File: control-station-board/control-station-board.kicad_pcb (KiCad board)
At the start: 2 copper layers, 9.7 x 10.3 mm, 41 parts, among them J1 USB_B, J2 USB_B, J3 CAM1_OUT, J4 CAM2_OUT, U1 MAX4445, U2 LTC1983ES6-5-TRPBF, U3 MAX4445, U4 THVD1550DR, U5 FT232RL, U6 ATA6560,1, U7 FT232RL

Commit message: working on pcb layout
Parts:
- removed R5, R6: 10k, Resistor_SMD:R_0603_1608Metric
- J1, J2: footprint Connector_USB:USB_B_OST_USB-B1HSxx_Horizontal -> Connector_USB:USB_B_TE_5787834_Vertical
- U4: value THVD1550DR -> MAX490E
- moved J3 137.7 mm to (168.6, 96.4), turned to 0 degrees
- moved J4 137.7 mm to (168.6, 80.4), turned to 0 degrees
- moved C6 117.4 mm to (155.8, 69.4), turned to 270 degrees
- moved C2 116.0 mm to (157.1, 99.7), turned to 270 degrees
- moved R3 115.9 mm to (157.0, 76.9), turned to 90 degrees
- moved R4 115.4 mm to (156.3, 74.6), turned to 180 degrees
- moved C4 114.3 mm to (155.1, 72.4), turned to 0 degrees
- moved R1 114.0 mm to (157.0, 93.1), turned to 90 degrees
- moved C7 114.0 mm to (157.0, 83.5), turned to 270 degrees
- moved R2 112.2 mm to (156.3, 90.8), turned to 180 degrees
- moved U2 112.0 mm to (153.0, 69.4), turned to 90 degrees
- moved C3 106.4 mm to (150.0, 69.5), turned to 90 degrees
- moved U1 105.7 mm to (152.3, 97.0), turned to 0 degrees
- moved U3 105.2 mm to (152.3, 80.9), turned to 0 degrees
- moved C5 104.0 mm to (150.4, 74.6), turned to 0 degrees
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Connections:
- R7 pad 1: RS485_B -> RX_H
- R7 pad 2: RS485_A -> RX_L
- U4 pad 1: R -> +5V
- U4 pad 2: Net-(R5-Pad1) -> R
- U4 pad 3: Net-(R6-Pad2) -> D
- U4 pad 4: D -> GND
- U4 pad 5: GND -> TX_H
- U4 pad 6: RS485_A -> TX_L
- U4 pad 7: RS485_B -> RX_L
- U4 pad 8: +5V -> RX_H
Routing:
- net GND: track 24.3 -> 26.8 mm
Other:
- board size 9.7 x 10.3 mm -> 76.2 x 44.5 mm

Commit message: Finishing pcb routing
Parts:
- added J5: USB D+/D-, Connector_PinHeader_2.54mm:PinHeader_1x02_P2.54mm_Vertical, F.Cu at (104.3, 90.6)
- added J6: Conn_02x06_Odd_Even, Connector_PinHeader_2.54mm:PinHeader_2x06_P2.54mm_Vertical, F.Cu at (104.3, 74.7)
- moved C6 37.8 mm to (149.6, 106.7), turned to 90 degrees
- moved R12 37.7 mm to (121.3, 94.0), turned to 180 degrees
- moved C3 37.5 mm to (155.5, 106.6), turned to 270 degrees
- moved D3 37.5 mm to (124.5, 94.0), turned to 0 degrees
- moved U2 37.3 mm to (152.5, 106.7), turned to 270 degrees
- moved R8 34.9 mm to (138.5, 94.1), turned to 180 degrees
- moved R13 33.4 mm to (121.4, 95.7), turned to 180 degrees
- moved D4 33.4 mm to (124.5, 95.7), turned to 0 degrees
- moved C4 31.7 mm to (150.3, 103.7), turned to 180 degrees
- moved R9 31.0 mm to (138.6, 95.6), turned to 180 degrees
- moved D1 30.5 mm to (141.8, 94.1), turned to 0 degrees
- moved D2 25.1 mm to (141.8, 95.6), turned to 0 degrees
- moved R10 24.4 mm to (120.8, 76.7), turned to 0 degrees
- moved C8 24.2 mm to (144.3, 81.4)
- moved R11 24.0 mm to (118.1, 80.4), turned to 90 degrees
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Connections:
- U5 pad 1: R -> D
- U5 pad 5: D -> R
- U7 pad 1: RXD -> TXD
- U7 pad 5: TXD -> RXD
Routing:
- net +5V: track 49.5 -> 208.3 mm, vias 5 -> 17
- net CAM1+: track 0.00 -> 64.4 mm, vias 0 -> 2
- net CAM1-: track 0.00 -> 63.1 mm, vias 0 -> 2
- net CAM2+: track 0.00 -> 53.7 mm, vias 0 -> 2
- net CAM2-: track 0.00 -> 50.3 mm, vias 0 -> 2
- net GND: track 26.8 -> 75.7 mm, vias 0 -> 44
- net RX_H: track 0.00 -> 32.4 mm, vias 0 -> 1
- net RX_L: track 0.00 -> 32.0 mm, vias 0 -> 1
- net TX_L: track 0.00 -> 31.3 mm, vias 0 -> 1
- net TX_H: track 0.00 -> 31.0 mm, vias 0 -> 1
- net CANL: track 0.00 -> 15.5 mm, vias 0 -> 1
- net CANH: track 0.00 -> 15.0 mm, vias 0 -> 1
- net Net-(J1-Pad3): track 0.00 -> 12.7 mm
- net Net-(J2-Pad3): track 0.00 -> 12.7 mm
- net Net-(J2-Pad2): track 0.00 -> 9.10 mm
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- added copper zone on B.Cu, net GND
- added copper zone on F.Cu, net GND
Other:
- board size 76.2 x 44.5 mm -> 68.6 x 43.8 mm

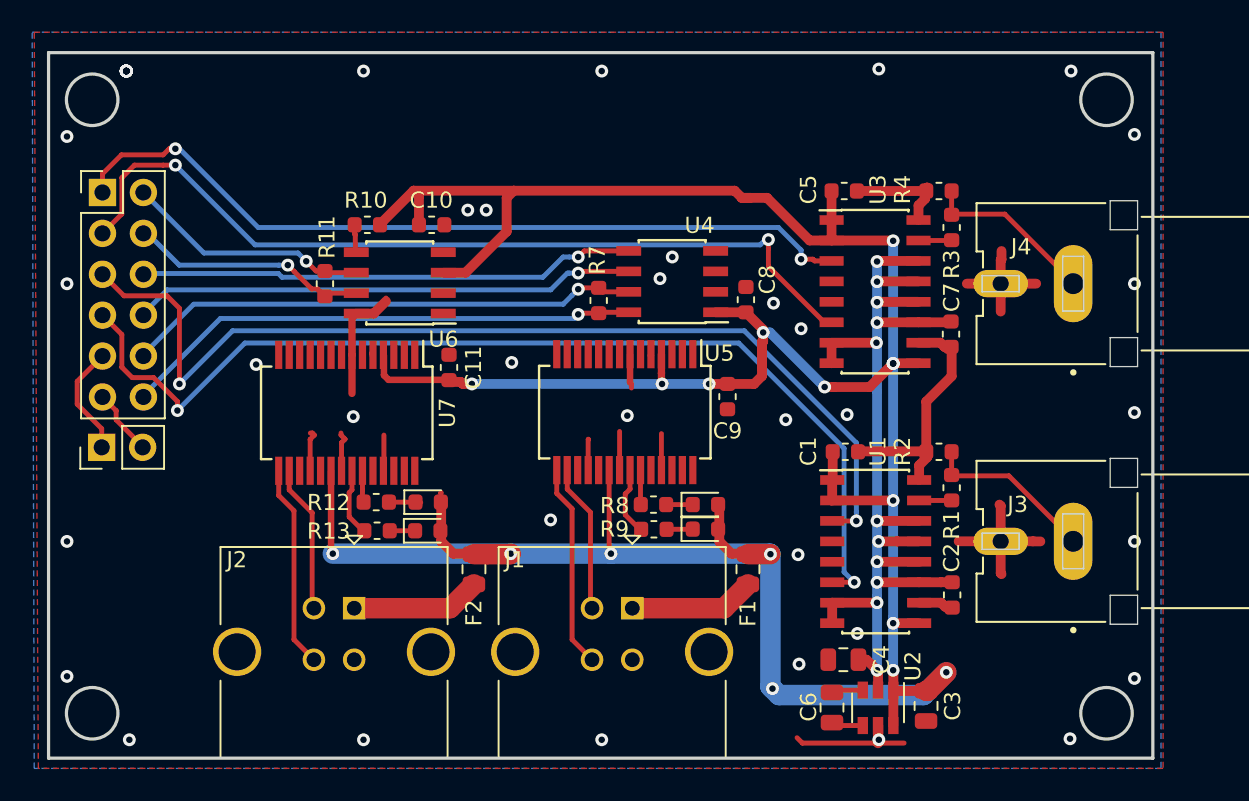
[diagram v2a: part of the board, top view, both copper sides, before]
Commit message: Finished PCB routing and silkscreen
Created 3d model,
Created gerber files
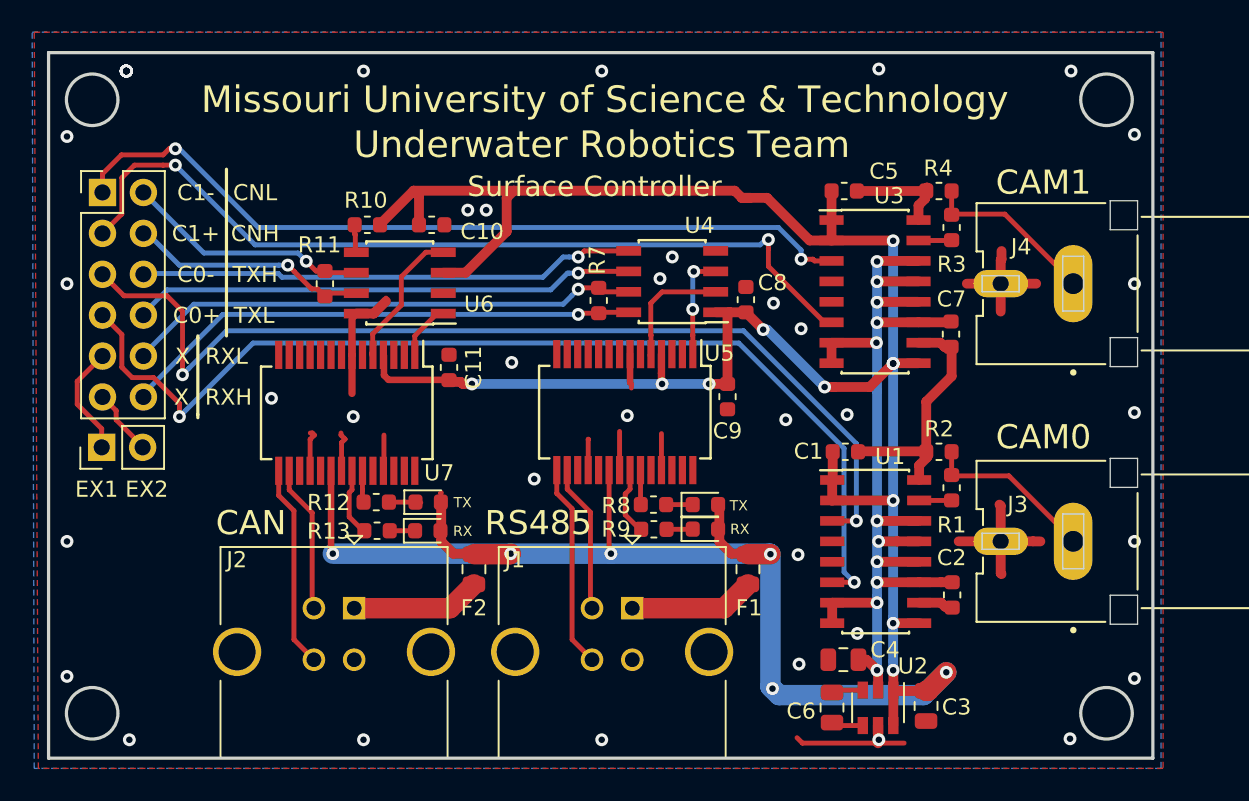
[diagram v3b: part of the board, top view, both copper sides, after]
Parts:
- J3: value CAM1_OUT -> CAM0_OUT
- J4: value CAM2_OUT -> CAM1_OUT
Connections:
- J3 pad 1: CAM1_OUT -> CAM0_OUT
- J4 pad 1: CAM2_OUT -> CAM1_OUT
- J6 pad 1: CAM2- -> CAM1-
- J6 pad 3: CAM2+ -> CAM1+
- J6 pad 5: CAM1- -> CAM0-
- J6 pad 7: CAM1+ -> CAM0+
- R1 pad 2: CAM1_OUT -> CAM0_OUT
- R2 pad 1: CAM1_OUT -> CAM0_OUT
- R3 pad 2: CAM2_OUT -> CAM1_OUT
- R4 pad 1: CAM2_OUT -> CAM1_OUT
- U1 pad 3: CAM1- -> CAM0-
- U1 pad 6: CAM1+ -> CAM0+
- U3 pad 3: CAM2- -> CAM1-
- U3 pad 6: CAM2+ -> CAM1+
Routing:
- net CAM0+: track 0.00 -> 64.9 mm, vias 0 -> 2
- net CAM0-: track 0.00 -> 62.2 mm, vias 0 -> 2
- net CAM2+: track 53.7 -> 0.00 mm, vias 2 -> 0
- net CAM2-: track 50.3 -> 0.00 mm, vias 2 -> 0
- net CAM1-: track 63.1 -> 50.3 mm
- net CAM2_OUT: track 10.8 -> 0.00 mm
- net CAM0_OUT: track 0.00 -> 10.8 mm
- net CAM1+: track 64.4 -> 53.7 mm
- net RXD: track 0.30 -> 9.09 mm
- net R: track 0.13 -> 7.65 mm
- net D: track 0.00 -> 6.63 mm, vias 0 -> 2
- net TXD: track 0.00 -> 3.46 mm
- net +5V: track 208.3 -> 206.0 mm
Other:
- board text added: "C0+"
- board text added: "C0-"
- board text added: "C1+"
- board text added: "C1-"
- board text added: "CAM0"
- board text added: "CAM1"
- board text added: "CAN"
- board text added: "CNH"
- board text added: "CNL"
- board text added: "EX1"
- board text added: "EX2"
- board text added: "Missouri University of Science & Technology"
- board text added: "RS485"
- board text added: "RX"
- board text added: "RXH"
- board text added: "RXL"
- board text added: "Surface Controller"
- board text added: "TX"
- board text added: "TXH"
- board text added: "TXL"
- board text added: "Underwater Robotics Team"
- board text added: "X"

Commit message: Exported gerber files for surface control board
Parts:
- added REF**: MountingHole_3.2mm_M3, MountingHole:MountingHole_3.2mm_M3, F.Cu at (103.7, 107.1)
- added REF**: MountingHole_3.2mm_M3, MountingHole:MountingHole_3.2mm_M3, F.Cu at (166.7, 107.1)
- added REF**: MountingHole_3.2mm_M3, MountingHole:MountingHole_3.2mm_M3, F.Cu at (166.6, 69.0)
- added REF**: MountingHole_3.2mm_M3, MountingHole:MountingHole_3.2mm_M3, F.Cu at (103.7, 69.0)
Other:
- outline, holes or cut-outs redrawn
- board text added: "Rev 1.0.0"
